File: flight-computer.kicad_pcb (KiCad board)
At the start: 2 copper layers, 50 x 62 mm, 53 parts, among them J1 Throttle/BEC, J2 Servo 1, J3 Servo 2, J4 Servo 3, J5 Servo 4, J6 Breakout1, J7 Power, J8 Ext, J9 Breakout2, SW1 SW_Push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

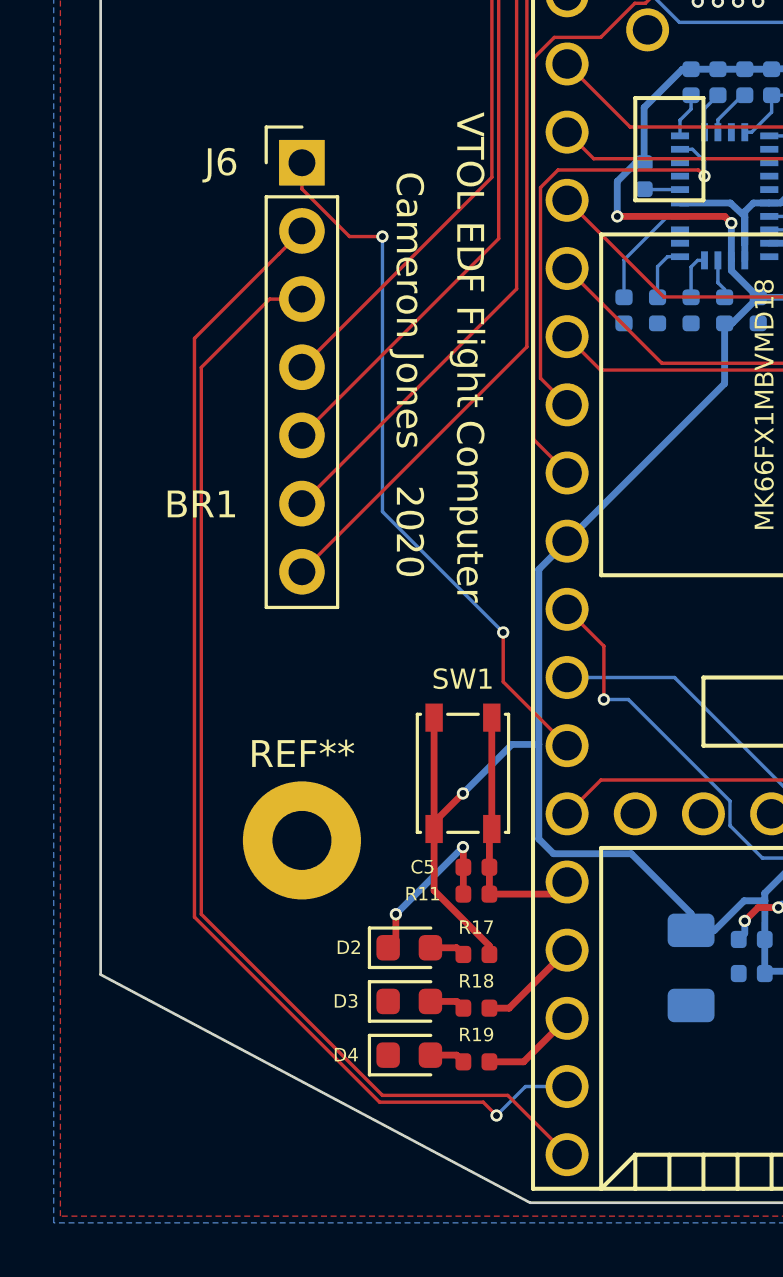
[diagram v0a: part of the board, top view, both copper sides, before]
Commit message: Re-routed a few traces
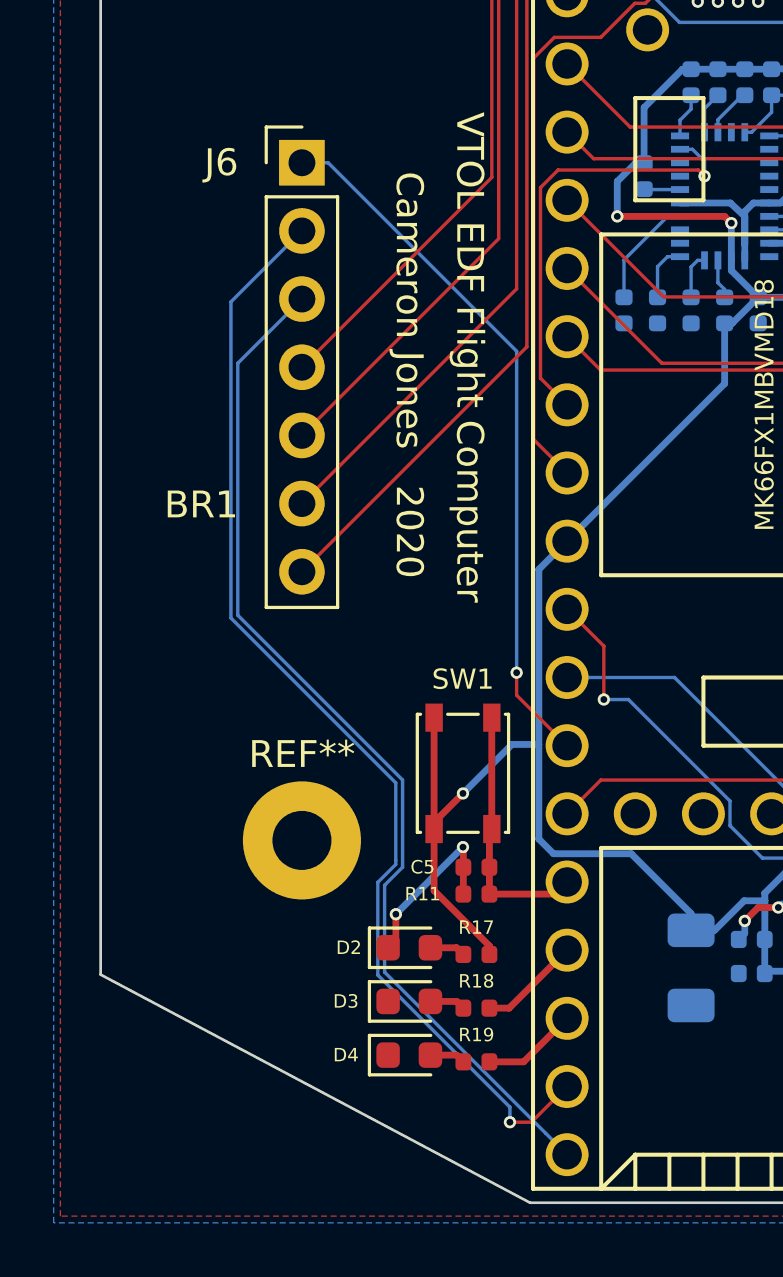
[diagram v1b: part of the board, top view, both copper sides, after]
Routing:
- net /D32: track 42.5 -> 38.5 mm
- net /D31: track 44.6 -> 41.8 mm
- net /D26: track 26.5 -> 26.4 mm, vias 2 -> 1

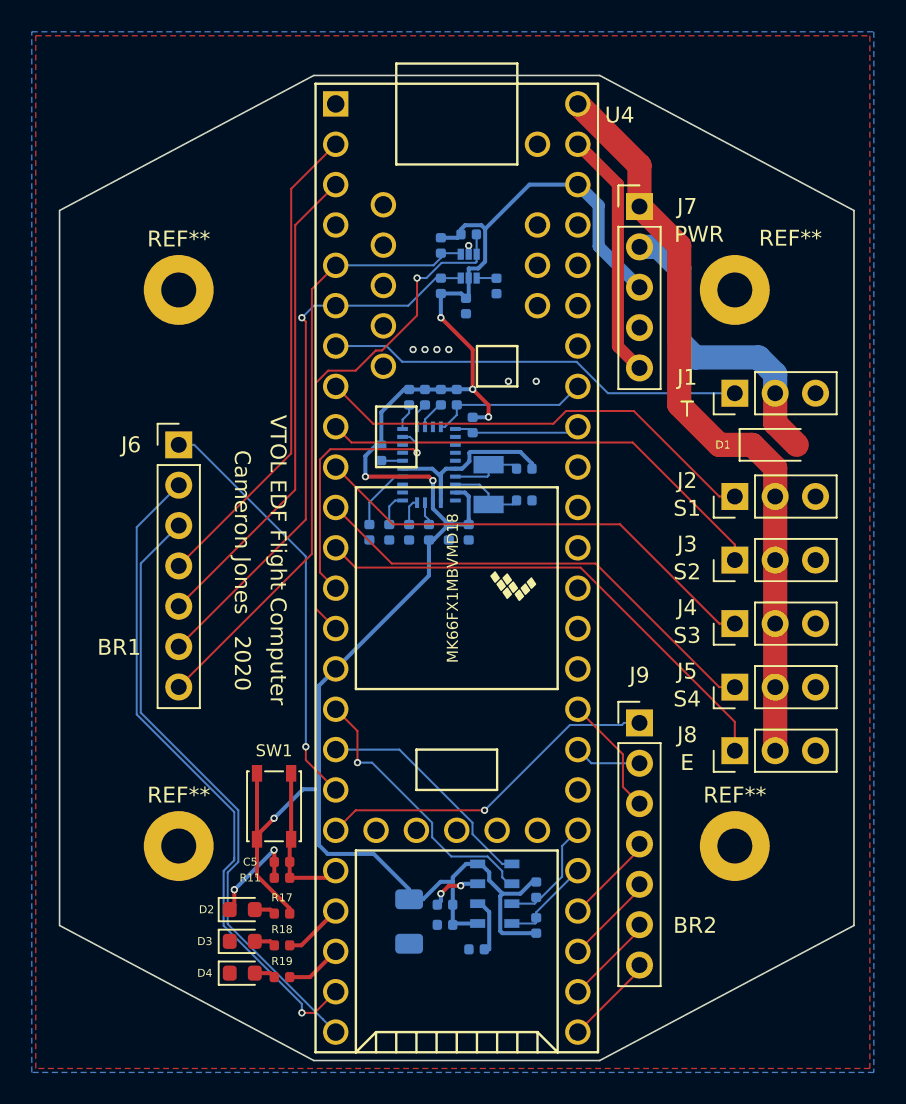
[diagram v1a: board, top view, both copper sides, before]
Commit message: Improved top silkscreen
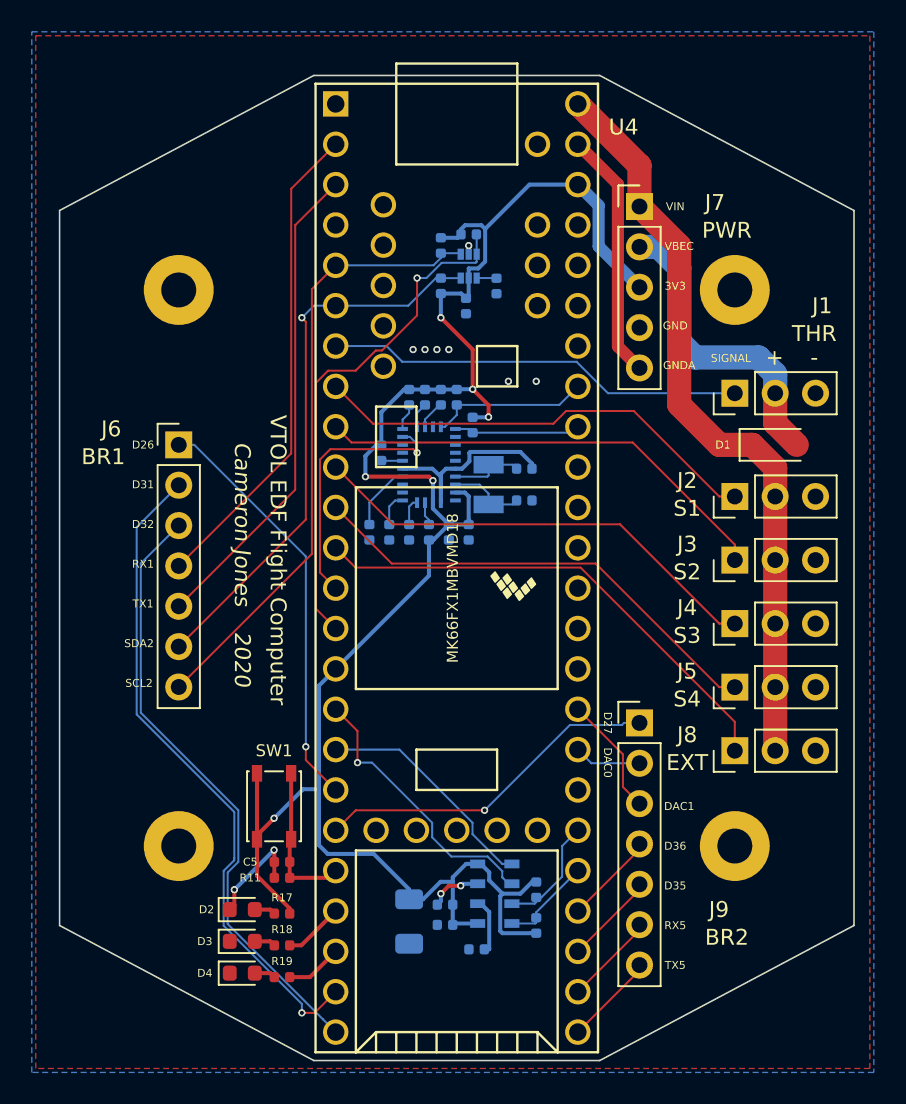
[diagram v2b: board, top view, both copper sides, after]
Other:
- board text added: "+"
- board text added: "-"
- board text added: "3V3"
- board text added: "D26"
- board text added: "D27"
- board text added: "D31"
- board text added: "D32"
- board text added: "D35"
- board text added: "D36"
- board text added: "DAC0"
- board text added: "DAC1"
- board text added: "EXT"
- board text added: "GND"
- board text added: "GNDA"
- board text added: "RX1"
- board text added: "RX5"
- board text added: "SCL2"
- board text added: "SDA2"
- board text added: "SIGNAL"
- board text added: "THR"
- board text added: "TX1"
- board text added: "TX5"
- board text added: "VBEC"
- board text added: "VIN"
- board text removed: "E"
- board text removed: "T"

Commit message: Cleaned up bottom silkscreen
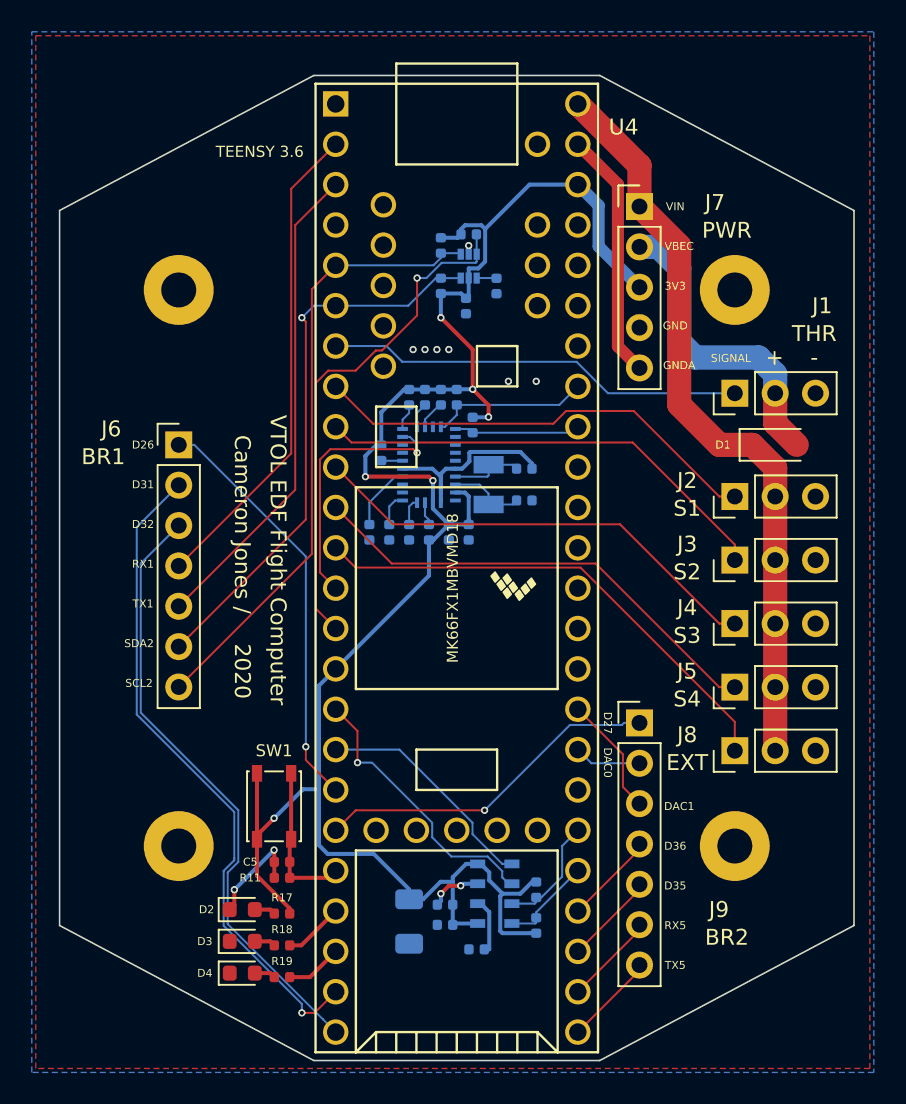
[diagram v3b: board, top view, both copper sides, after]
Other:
- board text added: "Cameron Jones /"
- board text added: "TEENSY 3.6"
- board text removed: "Cameron Jones"

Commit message: Easter egg
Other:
- board text added: "Gatsby"
- board text added: "Gnocchi"
- board text added: "Gobi"
- board text added: "Gryphon"
- board text added: "Loki"
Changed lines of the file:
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@@
   (general
     (thickness 1.6)
-    (drawings 44)
+    (drawings 49)
     (tracks 369)
     (zones 0)
@@
       (rotate (xyz 0 0 0))
     )
+  )
+  (gr_text Loki (at 107 54.6) (layer F.Cu)
+    (effects (font (size 0.6 0.6) (thickness 0.15)) (justify left))
+  )
+  (gr_text Gnocchi (at 107 53.8) (layer F.Cu)
+    (effects (font (size 0.6 0.6) (thickness 0.15)) (justify left))
+  )
+  (gr_text Gobi (at 107 53) (layer F.Cu)
+    (effects (font (size 0.6 0.6) (thickness 0.15)) (justify left))
+  )
+  (gr_text Gatsby (at 107 52.2) (layer F.Cu)
+    (effects (font (size 0.6 0.6) (thickness 0.15)) (justify left))
+  )
+  (gr_text Gryphon (at 107 51.4) (layer F.Cu)
+    (effects (font (size 0.6 0.6) (thickness 0.15)) (justify left))
   )
   (gr_text "TEENSY 3.6" (at 96.6 54.8) (layer F.SilkS)
@@
     (connect_pads (clearance 0.3))
     (min_thickness 0.254)
-    (fill (arc_segments 32) (thermal_gap 0.508) (thermal_bridge_width 0.508))
+    (fill yes (arc_segments 32) (thermal_gap 0.508) (thermal_bridge_width 0.508))
     (polygon
       (pts
@@
     (connect_pads (clearance 0.3))
     (min_thickness 0.254)
-    (fill (arc_segments 32) (thermal_gap 0.508) (thermal_bridge_width 0.508))
+    (fill yes (arc_segments 32) (thermal_gap 0.508) (thermal_bridge_width 0.508))
     (polygon
       (pts
@@
       )
     )
+  )
+  (zone (net 0) (net_name "") (layer F.Cu) (hatch edge 0.508)
+    (connect_pads (clearance 0.3))
+    (min_thickness 0.254)
+    (keepout (tracks not_allowed) (vias not_allowed) (copperpour not_allowed))
+    (fill (arc_segments 32) (thermal_gap 0.508) (thermal_bridge_width 0.508))
+    (polygon
+      (pts
+        (xy 112.81 55.6) (xy 105.19 55.6) (xy 105.19 49.25) (xy 112.81 49.25)
+      )
+    )

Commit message: Version number and mounting hole reference designators
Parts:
- renumbered REF** to MH1, REF** to MH2, REF** to MH3, REF** to MH4
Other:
- board text added: "V1"
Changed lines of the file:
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@@
   (general
     (thickness 1.6)
-    (drawings 49)
+    (drawings 50)
     (tracks 369)
     (zones 0)
@@
     (tags "mounting hole 2.2mm m2")
     (attr virtual)
-    (fp_text reference REF** (at 3.5 -3.25) (layer F.SilkS) hide
+    (fp_text reference MH2 (at 3.5 -3.25) (layer F.SilkS) hide
       (effects (font (size 1 1) (thickness 0.15)))
     )
@@
     (tags "mounting hole 2.2mm m2")
     (attr virtual)
-    (fp_text reference REF** (at 0 -3.2) (layer F.SilkS) hide
+    (fp_text reference MH1 (at 0 -3.2) (layer F.SilkS) hide
       (effects (font (size 1 1) (thickness 0.15)))
     )
@@
     (tags "mounting hole 2.2mm m2")
     (attr virtual)
-    (fp_text reference REF** (at 0 -3.2) (layer F.SilkS) hide
+    (fp_text reference MH3 (at 0 -3.2) (layer F.SilkS) hide
       (effects (font (size 1 1) (thickness 0.15)))
     )
@@
     (tags "mounting hole 2.2mm m2")
     (attr virtual)
-    (fp_text reference REF** (at 0 -3.2) (layer F.SilkS) hide
+    (fp_text reference MH4 (at 0 -3.2) (layer F.SilkS) hide
       (effects (font (size 1 1) (thickness 0.15)))
     )
@@
     )
   )
+  (gr_text V1 (at 95.2 58.6) (layer F.SilkS)
+    (effects (font (size 1.5 1.5) (thickness 0.3)))
+  )
   (gr_text Loki (at 107 54.6) (layer F.Cu)
